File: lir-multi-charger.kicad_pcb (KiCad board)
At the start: 2 copper layers, 90 x 58 mm, 54 parts, among them J1 USB_C_Receptacle_USB2.0, J11 Conn_01x01_Male, J12 Conn_01x01_Male, J2 Conn_01x02_Male, J3 Conn_01x02_Male, J4 Conn_01x02_Male, J5 Conn_01x02_Male, J6 Conn_01x02_Male, U1 CN3130, U2 CN3130, U3 CN3130

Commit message: gerbers single
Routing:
- net GND: track 0.00 -> 257.1 mm
- net Net-(R15-Pad2): track 0.00 -> 100.6 mm
- net Net-(R5-Pad2): track 0.00 -> 78.5 mm
- net Net-(C3-Pad1): track 0.00 -> 66.1 mm
- net VBUS: track 0.00 -> 47.9 mm
- net Net-(R16-Pad1): track 0.00 -> 45.5 mm
- net Net-(R3-Pad2): track 0.00 -> 45.4 mm
- net Net-(R8-Pad2): track 0.00 -> 44.2 mm
- net Net-(R13-Pad2): track 0.00 -> 40.6 mm, vias 0 -> 2
- net Net-(C4-Pad1): track 0.00 -> 39.6 mm, vias 0 -> 1
- net Net-(C6-Pad1): track 0.00 -> 39.4 mm
- net Net-(C2-Pad1): track 0.00 -> 26.2 mm
- net unconnected-(J1-PadS1): track 0.00 -> 17.0 mm
- net Net-(D2-Pad2): track 0.00 -> 15.9 mm
- net Net-(R6-Pad1): track 0.00 -> 14.6 mm
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
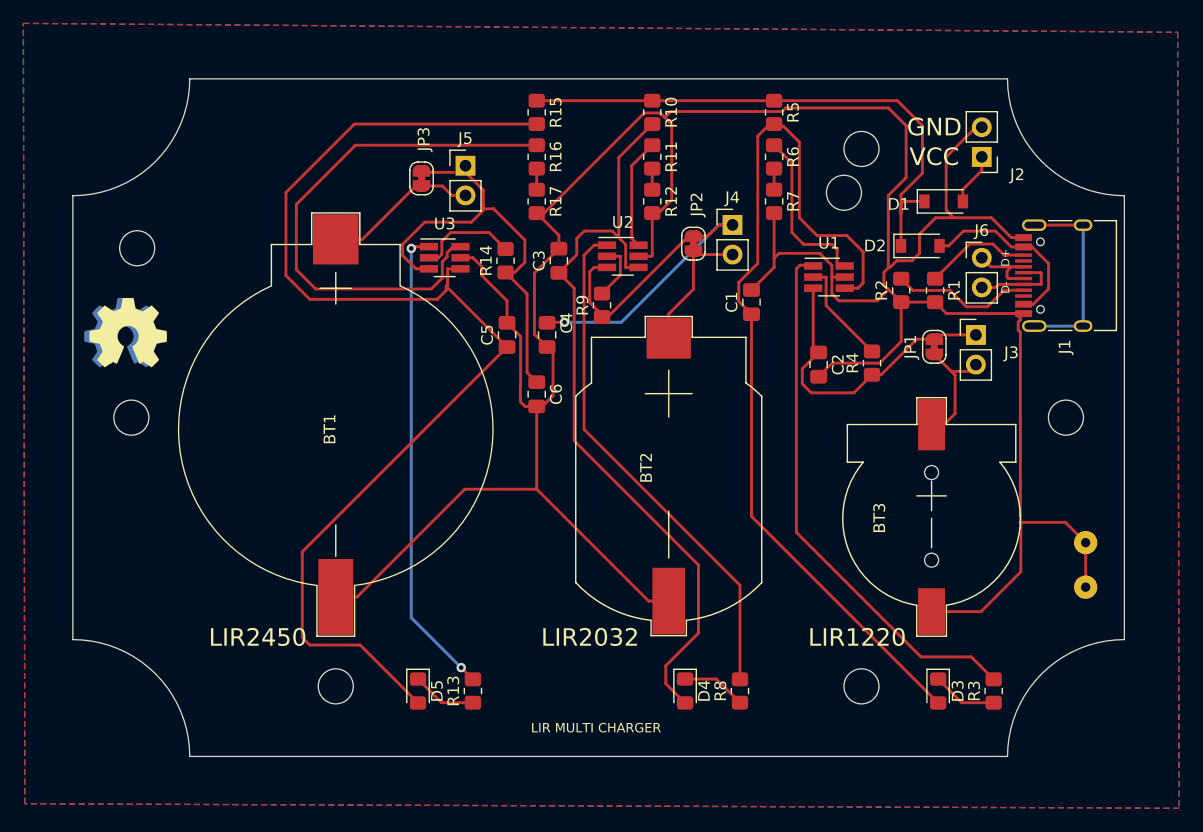
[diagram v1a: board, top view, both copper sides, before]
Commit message: upgraded kicad version to 9, starting to add ext bat connectors
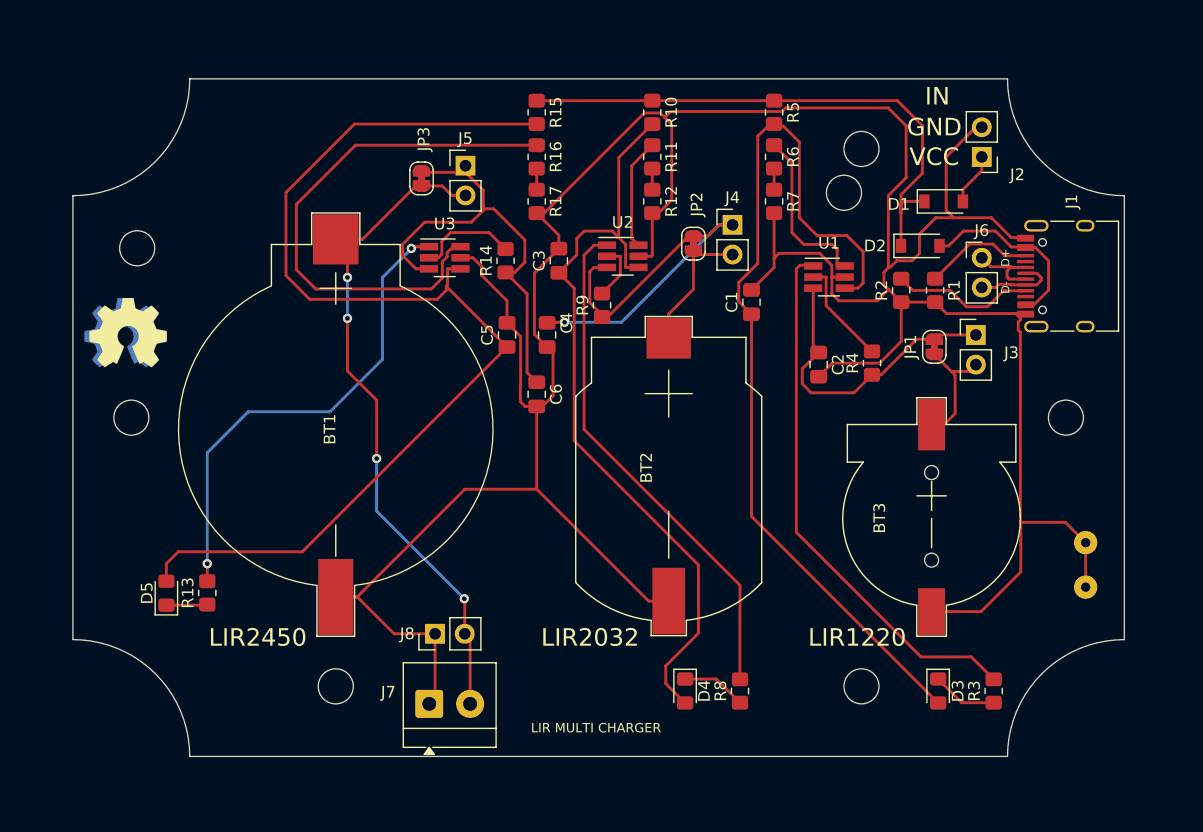
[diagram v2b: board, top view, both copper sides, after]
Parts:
- added J7: Screw_Terminal_01x02, TerminalBlock_4Ucon:TerminalBlock_4Ucon_1x02_P3.50mm_Horizontal, F.Cu at (130.5, 153.5)
- added J8: Conn_01x02_Pin, Connector_PinHeader_2.54mm:PinHeader_1x02_P2.54mm_Vertical, F.Cu at (131.0, 147.5)
- moved R13 24.2 mm to (111.5, 144.0)
- moved D5 23.1 mm to (108.0, 144.0), turned to 90 degrees
- moved J1 0.19 mm to (185.6, 116.9)
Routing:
- net Net-(BT1-+): track 13.3 -> 61.8 mm, vias 0 -> 4
- net unconnected-(J1-SHIELD-PadS1)_3: track 17.0 -> 0.00 mm
- net GND: track 257.1 -> 273.1 mm
- net Net-(D5-A): track 100.6 -> 94.6 mm
- net Net-(D5-K): track 5.54 -> 3.52 mm
- net Net-(U3-/CHRG): track 40.6 -> 41.4 mm
- net Net-(J6-Pin_2): track 7.70 -> 7.10 mm
- net Net-(D2-A): track 15.9 -> 16.4 mm
- removed copper zone on B.Cu, net GND
- removed copper zone on F.Cu, net GND
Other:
- board text added: "IN"

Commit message: Revert "upgraded kicad version to 9, starting to add ext bat connectors"
This reverts commit a6eeaf41d868e39ea5ead22df93e0c5d5fe9c91a.
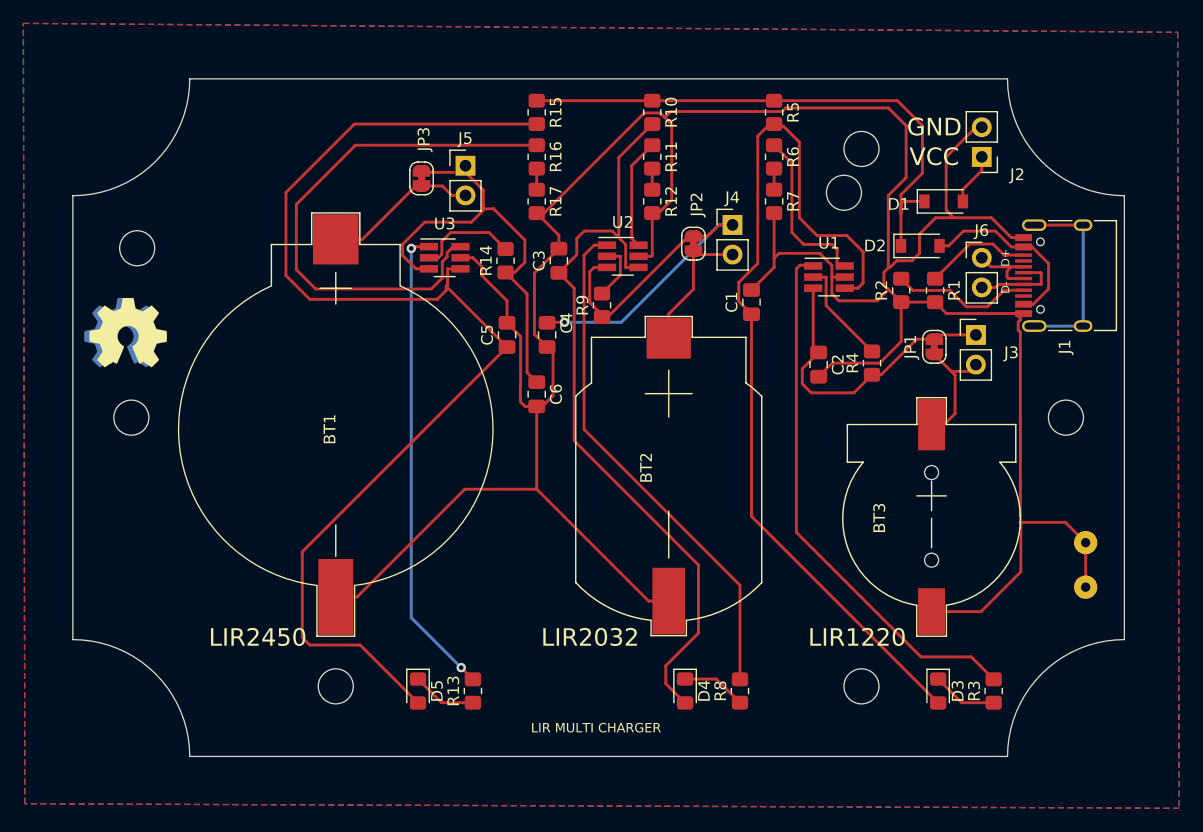
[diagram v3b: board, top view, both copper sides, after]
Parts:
- removed J7: Screw_Terminal_01x02, TerminalBlock_4Ucon:TerminalBlock_4Ucon_1x02_P3.50mm_Horizontal
- removed J8: Conn_01x02_Pin, Connector_PinHeader_2.54mm:PinHeader_1x02_P2.54mm_Vertical
- moved R13 24.2 mm to (134.2, 152.4)
- moved D5 23.1 mm to (129.5, 152.4), turned to -90 degrees
- moved J1 0.19 mm to (185.4, 116.8)
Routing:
- net Net-(BT1-Pad1): track 61.8 -> 13.3 mm, vias 4 -> 0
- net unconnected-(J1-PadS1): track 0.00 -> 17.0 mm
- net GND: track 273.1 -> 257.1 mm
- net Net-(R15-Pad2): track 94.6 -> 100.6 mm
- net Net-(D5-Pad1): track 3.52 -> 5.54 mm
- net Net-(R13-Pad2): track 41.4 -> 40.6 mm
- net Net-(J1-PadA7): track 7.10 -> 7.70 mm
- net Net-(D2-Pad2): track 16.4 -> 15.9 mm
- added copper zone on B.Cu, net GND
- added copper zone on F.Cu, net GND
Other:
- board text removed: "IN"

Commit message: Update PCB design for KiCad 7 compatibility and add external battery connector
- Migrated project from KiCad 6 to KiCad 7
- Updated library links and component references for KiCad 7 compatibility
- Added external battery connector terminal block
- Updated project files (.kicad_pro, .kicad_prl, .kicad_sch, .kicad_pcb)
- Updated footprint info cache for new component references
- Added new backup files from recent design iterations
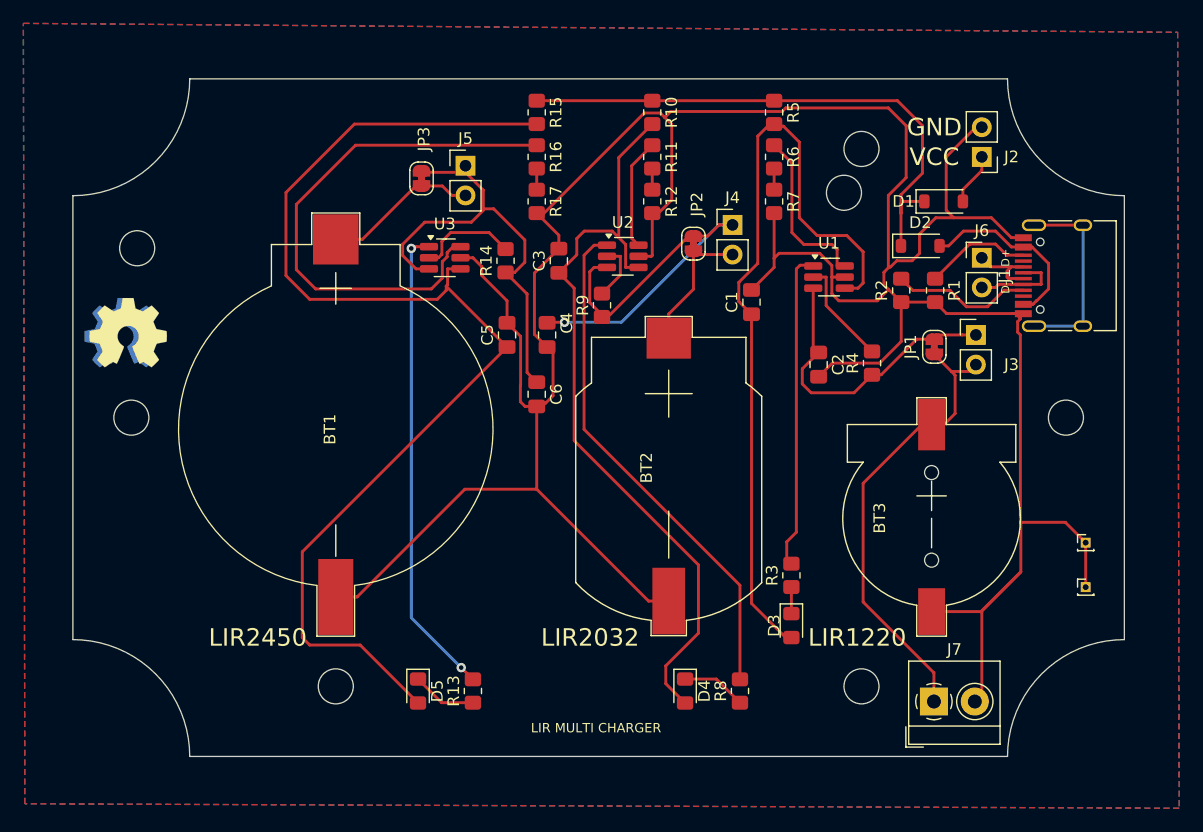
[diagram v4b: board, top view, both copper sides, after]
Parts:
- removed J11, J12: Conn_01x01_Male, Connector_Wire:SolderWirePad_1x01_Drill0.8mm
- added J7: Conn_01x02_Socket, TerminalBlock_4Ucon:TerminalBlock_4Ucon_1x02_P3.50mm_Horizontal, F.Cu at (173.7, 153.3)
- added REF**: PinHeader_1x01_P1.00mm_Vertical, Connector_PinHeader_1.00mm:PinHeader_1x01_P1.00mm_Vertical, F.Cu at (186.7, 139.7)
- added REF**: PinHeader_1x01_P1.00mm_Vertical, Connector_PinHeader_1.00mm:PinHeader_1x01_P1.00mm_Vertical, F.Cu at (186.7, 143.5)
- J1: value USB_C_Receptacle_USB2.0 -> USB_C_Receptacle_USB2.0_16P
- J2, J3, J4, J5, J6: value Conn_01x02_Male -> Conn_01x02_Pin
- moved R3 19.9 mm to (161.5, 142.5)
- moved D3 13.8 mm to (161.5, 146.8)
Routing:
- net Net-(BT3-+): track 10.9 -> 40.0 mm
- net Net-(U1-/CHRG): track 45.4 -> 26.3 mm
- net GND: track 257.1 -> 272.1 mm
- net Net-(D3-A): track 78.5 -> 68.0 mm
- net Net-(D3-K): track 5.59 -> 2.28 mm

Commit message: Add two screw terminal blocks for external battery connections
- Added TB1 and TB2 terminal blocks to schematic for external battery charging
- Routed PCB layout with new terminal block components
- Connected terminals to power rails for battery input
- Enables external battery charging capability
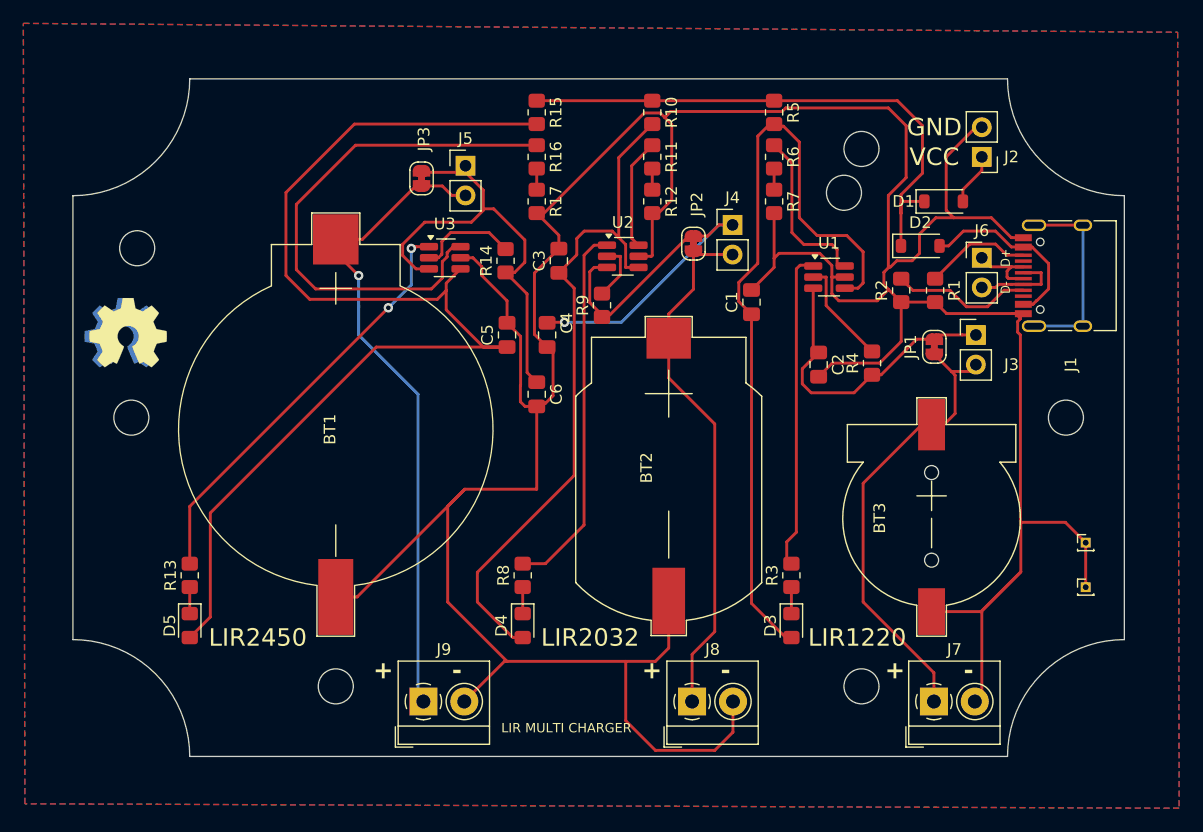
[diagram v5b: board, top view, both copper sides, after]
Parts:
- added J8: Conn_01x02_Socket, TerminalBlock_4Ucon:TerminalBlock_4Ucon_1x02_P3.50mm_Horizontal, F.Cu at (153.0, 153.3)
- added J9: Conn_01x02_Socket, TerminalBlock_4Ucon:TerminalBlock_4Ucon_1x02_P3.50mm_Horizontal, F.Cu at (130.0, 153.3)
- moved R13 26.2 mm to (110.0, 142.5)
- moved R8 21.1 mm to (138.5, 142.5)
- moved D5 20.3 mm to (110.0, 146.8)
- moved D4 15.0 mm to (138.5, 146.8)
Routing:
- net GND: track 272.1 -> 316.3 mm
- net Net-(BT1-+): track 13.3 -> 56.2 mm, vias 0 -> 1
- net Net-(BT2-+): track 11.7 -> 45.2 mm
- net Net-(U2-/CHRG): track 44.2 -> 32.0 mm
- net Net-(D4-A): track 66.1 -> 59.8 mm
- net Net-(U3-/CHRG): track 40.6 -> 36.4 mm
- net Net-(D5-K): track 5.54 -> 2.28 mm
- net Net-(D4-K): track 5.54 -> 2.28 mm
- net Net-(D5-A): track 100.6 -> 99.1 mm
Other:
- board text added: "+ -"
